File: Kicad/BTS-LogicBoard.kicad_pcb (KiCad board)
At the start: 2 copper layers, 41.9 x 55.9 mm, 52 parts, among them J1 Conn_01x06, J2 Conn_01x04, J3 Conn_01x02, Q1 BC817, Q2 BC807, Q3 BC817, Q4 BC807, Q5 BC817, Q6 BC817, SW1 SW_DPDT_x2, SW2 SW_DPDT_x2, U1 NCS2252SN2T1G, U2 NE555D, U3 NCS2252SN2T1G

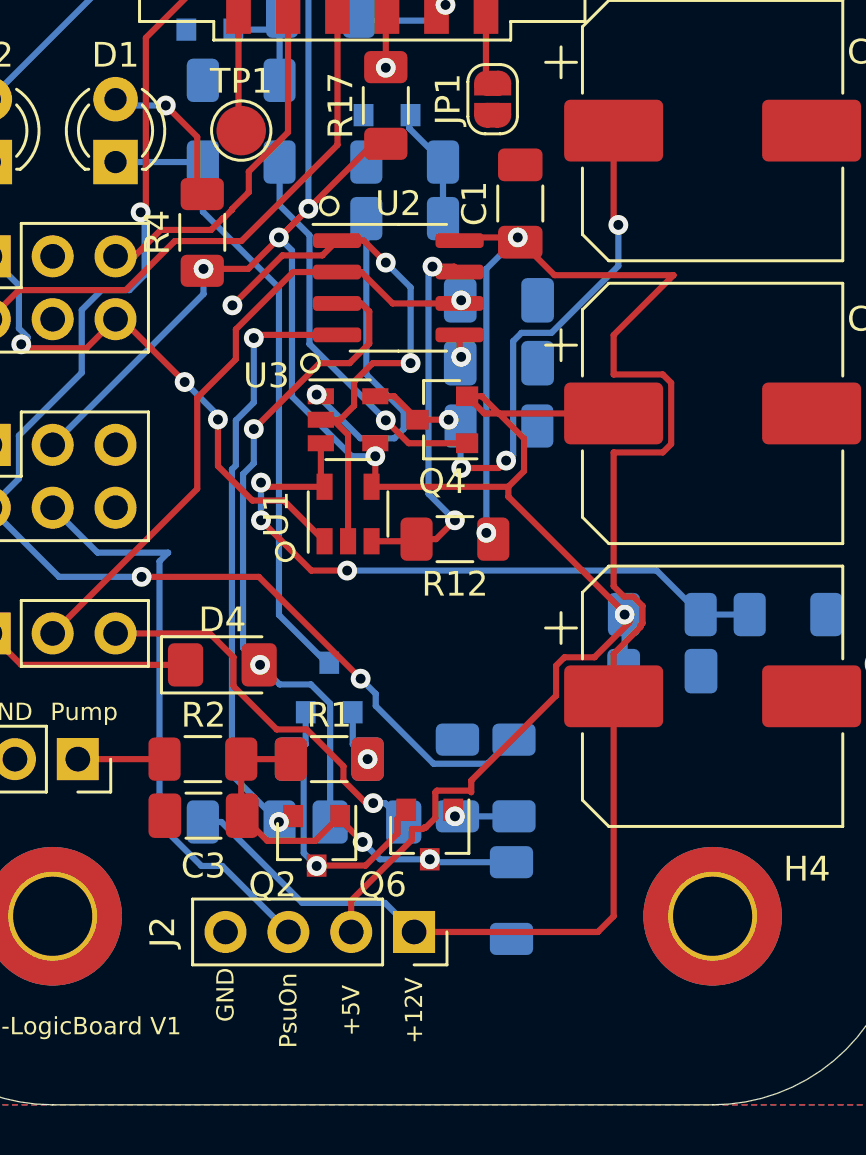
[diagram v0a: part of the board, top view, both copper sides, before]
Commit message: Updated silkscreen and Gerbers
Signed-off-by: bebenlebricolo <benoittarrade@hotmail.fr>
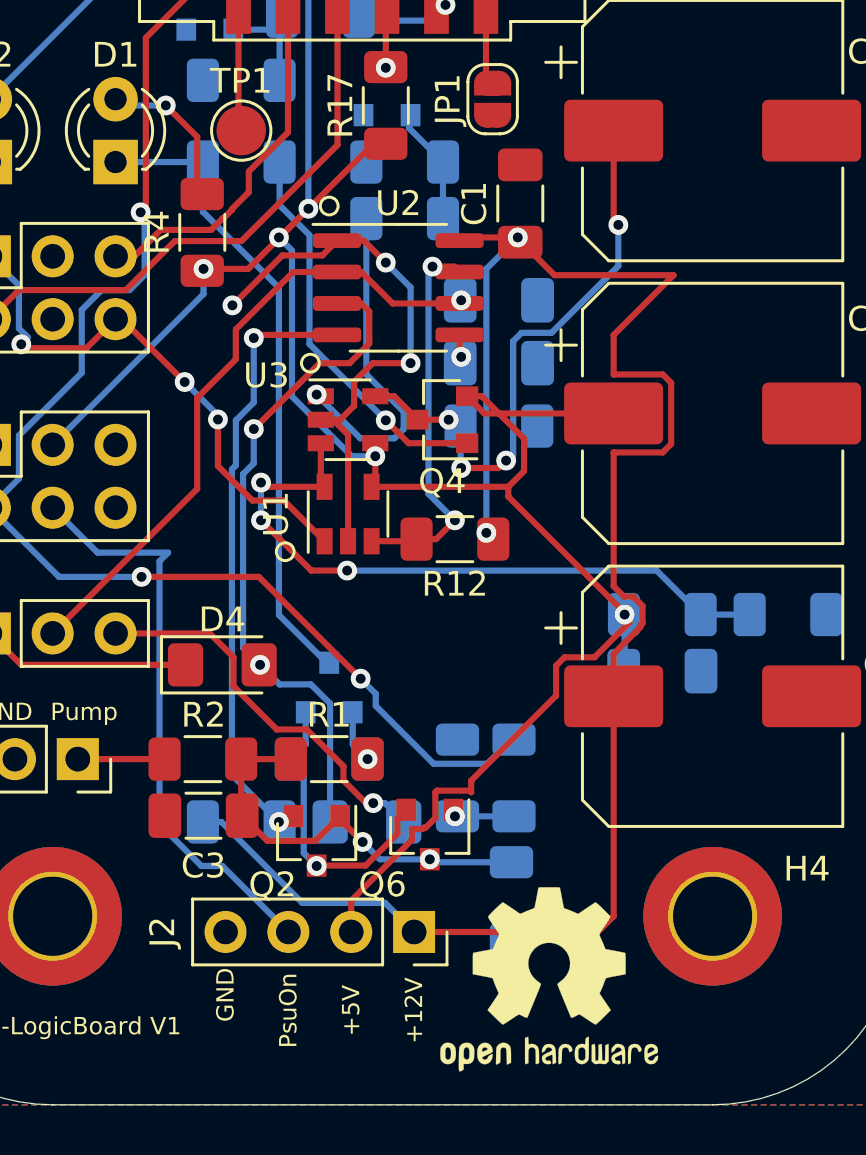
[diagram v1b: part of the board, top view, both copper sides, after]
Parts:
- added REF**: OSHW-Logo2_9.8x8mm_SilkScreen, Symbol:OSHW-Logo2_9.8x8mm_SilkScreen, B.Cu at (141.0, 81.5)
- added REF**: OSHW-Logo2_9.8x8mm_SilkScreen, Symbol:OSHW-Logo2_9.8x8mm_SilkScreen, F.Cu at (139.4, 116.8)

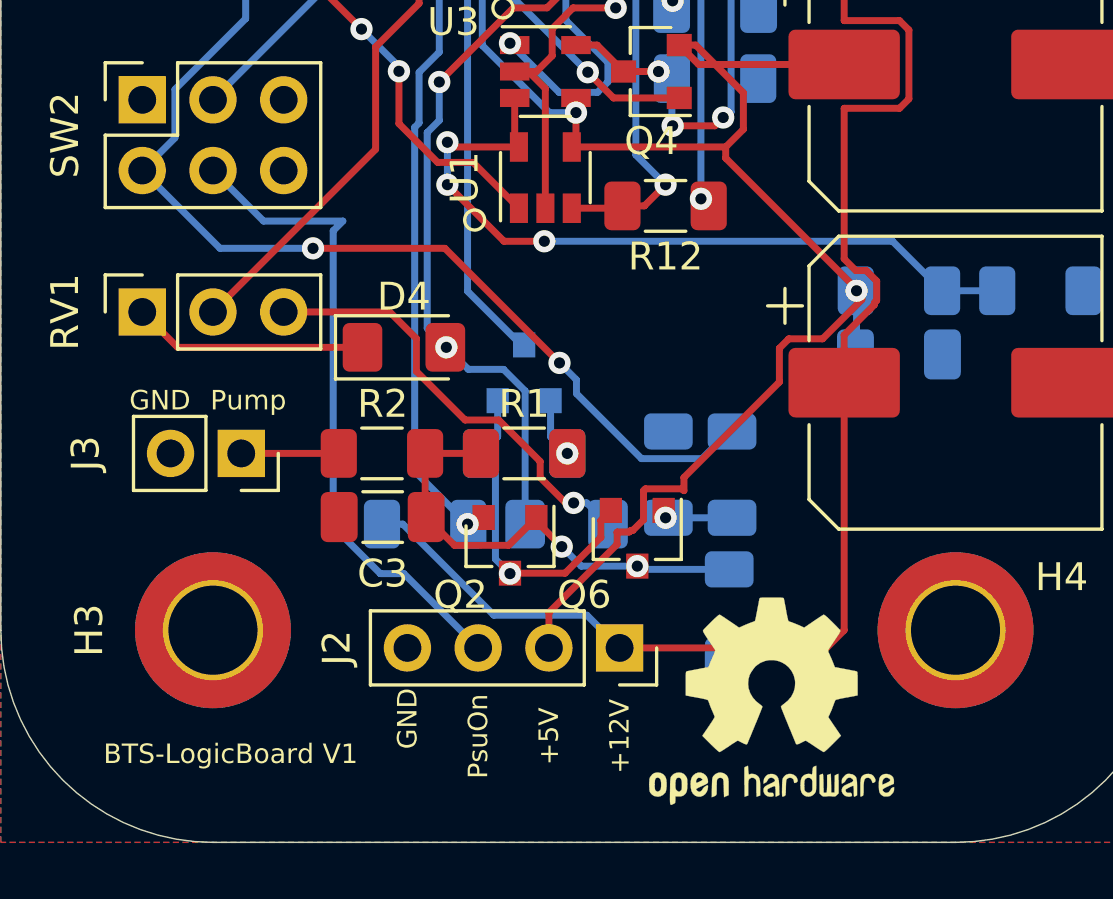
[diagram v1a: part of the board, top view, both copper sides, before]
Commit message: Updated board with optocoupler
Signed-off-by: bebenlebricolo <benoittarrade@hotmail.fr>
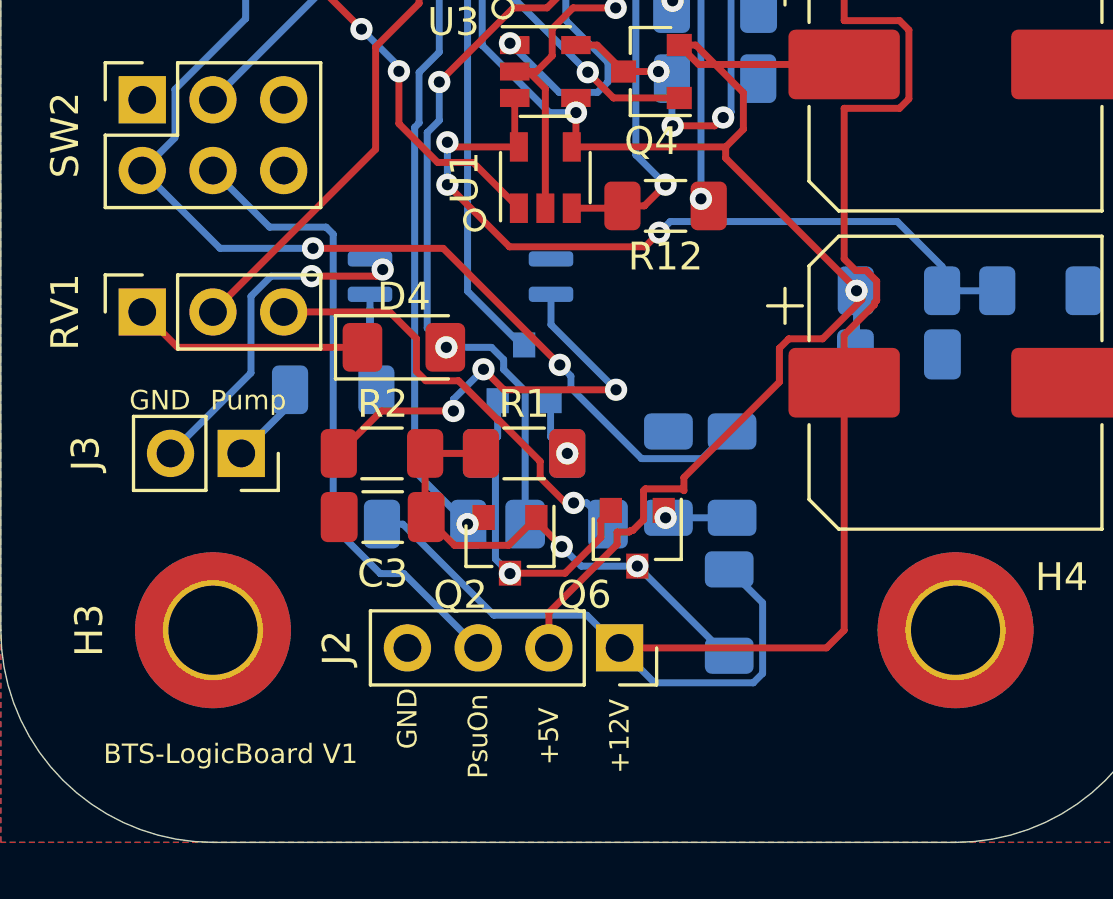
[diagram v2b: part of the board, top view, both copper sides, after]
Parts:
- removed REF** (x2): OSHW-Logo2_9.8x8mm_SilkScreen, Symbol:OSHW-Logo2_9.8x8mm_SilkScreen
- added R20: 1k, Resistor_SMD:R_1206_3216Metric_Pad1.30x1.75mm_HandSolder, B.Cu at (123.7, 105.7)
- added U4: TLP291, Package_SO:SOIC-4_4.55x2.6mm_P1.27mm, B.Cu at (128.3, 101.6)
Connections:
- J3 pad 2: GND -> GND1
- R2 pad 2: /Pump-On -> Net-(R2-Pad2)
- R5 pad 1: /PWM_Enable -> +12V
- R5 pad 2: GND -> /PWM_Enable
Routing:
- net Net-(R2-Pad2): track 0.00 -> 16.2 mm, vias 0 -> 3
- net GND1: track 0.00 -> 12.6 mm, vias 0 -> 2
- net +12V: track 73.2 -> 83.3 mm
- net Net-(R20-Pad1): track 0.00 -> 6.22 mm
- net /PWM_Enable: track 16.9 -> 18.3 mm
- net /2.5V: track 27.3 -> 28.6 mm
- net /PSU_ON: track 23.5 -> 22.8 mm

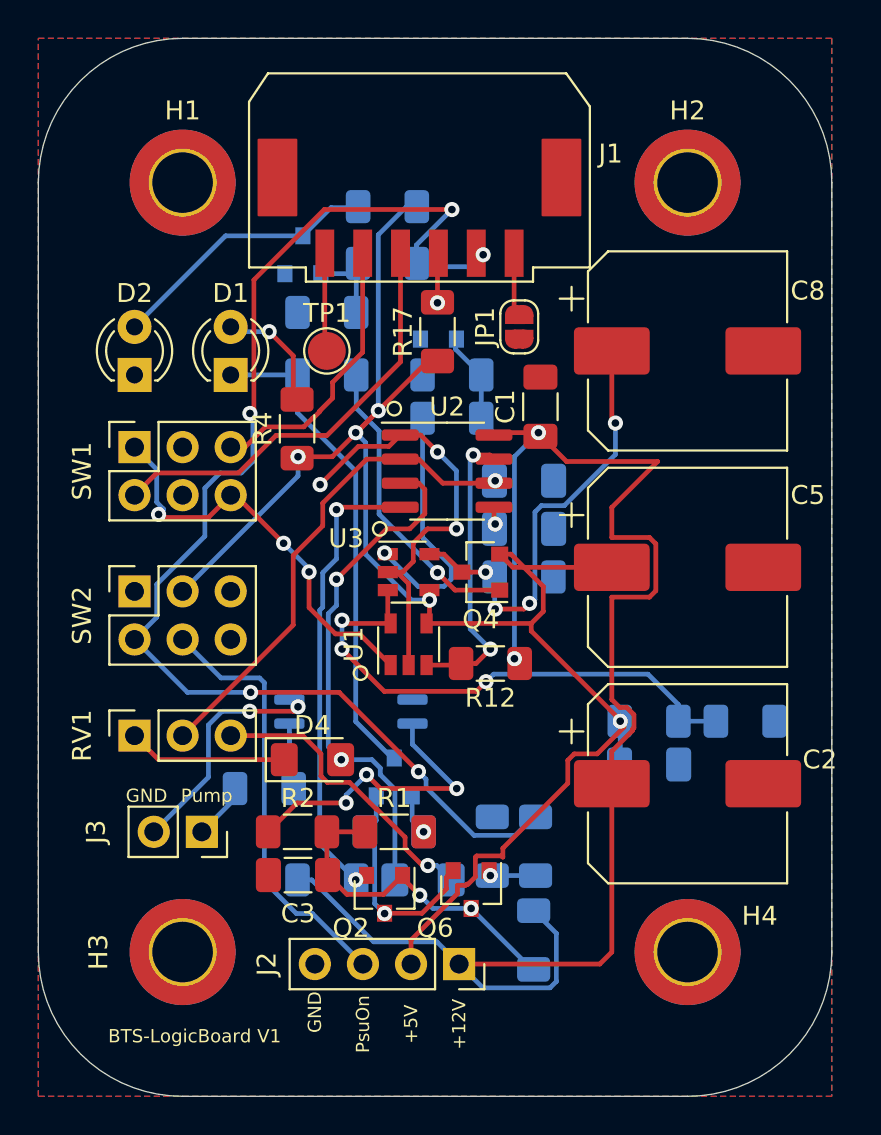
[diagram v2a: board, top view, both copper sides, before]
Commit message: Fixed unatural DPDT switch mapping
Signed-off-by: bebenlebricolo <benoittarrade@hotmail.fr>
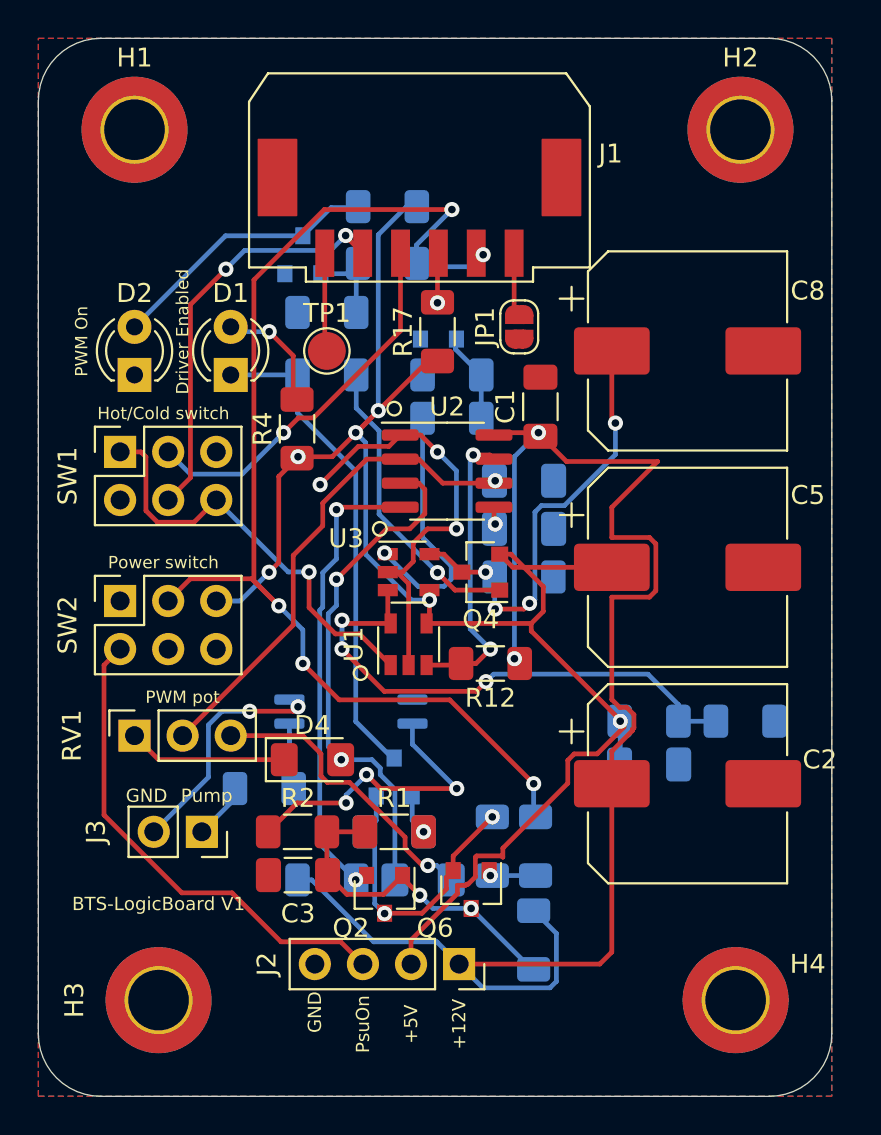
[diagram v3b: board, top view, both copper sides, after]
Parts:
- SW1, SW2: footprint Connector_PinSocket_2.54mm:PinSocket_2x03_P2.54mm_Vertical -> BTS-LogicBoard:PinSocket_2x03_P2.54mm_Vertical_DPDT_Special
- moved H2 3.95 mm to (148.8, 70.9)
- moved H1 3.78 mm to (116.8, 70.9)
- moved H4 3.59 mm to (148.6, 116.8)
- moved H3 2.84 mm to (118.1, 116.8)
- moved SW2 0.92 mm to (116.1, 95.8)
- moved SW1 0.80 mm to (116.1, 87.9)
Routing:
- net /IN-: track 14.8 -> 21.8 mm, vias 0 -> 2
- net GND: track 34.4 -> 38.1 mm, vias 4 -> 5
- net /HIP_DISABLE: track 68.4 -> 64.9 mm
- net /PSU_ON: track 22.8 -> 26.1 mm
- net /IN+: track 22.7 -> 20.0 mm, vias 0 -> 1
- net /COMP-Out: track 22.0 -> 22.9 mm, vias 3 -> 1
- net +5V: track 92.2 -> 92.6 mm, vias 5 -> 6
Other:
- outline, holes or cut-outs redrawn
- board text added: "Driver Enabled"
- board text added: "Hot/Cold switch"
- board text added: "PWM On"
- board text added: "PWM pot"
- board text added: "Power switch"

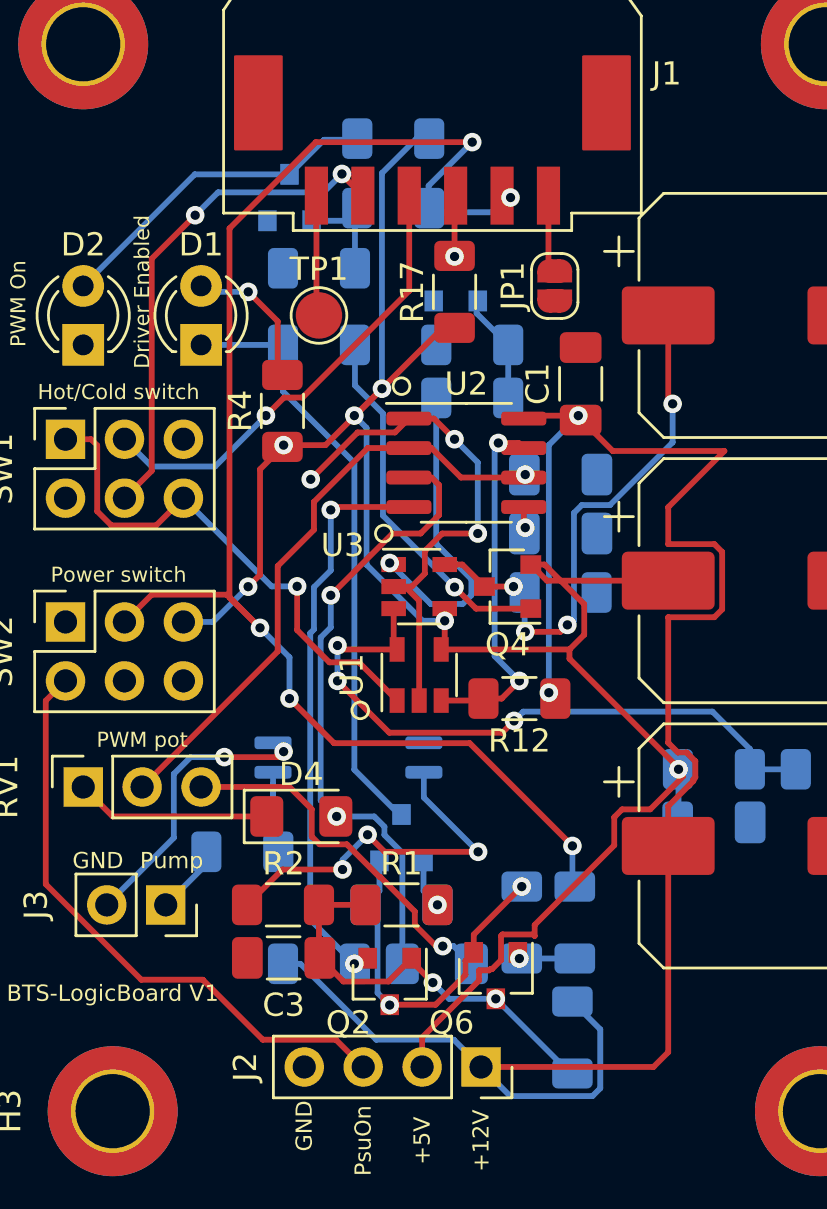
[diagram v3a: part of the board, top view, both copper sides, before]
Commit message: Swapped 12Vcc on NE555 outputs and remapped comparators
Signed-off-by: bebenlebricolo <benoittarrade@hotmail.fr>
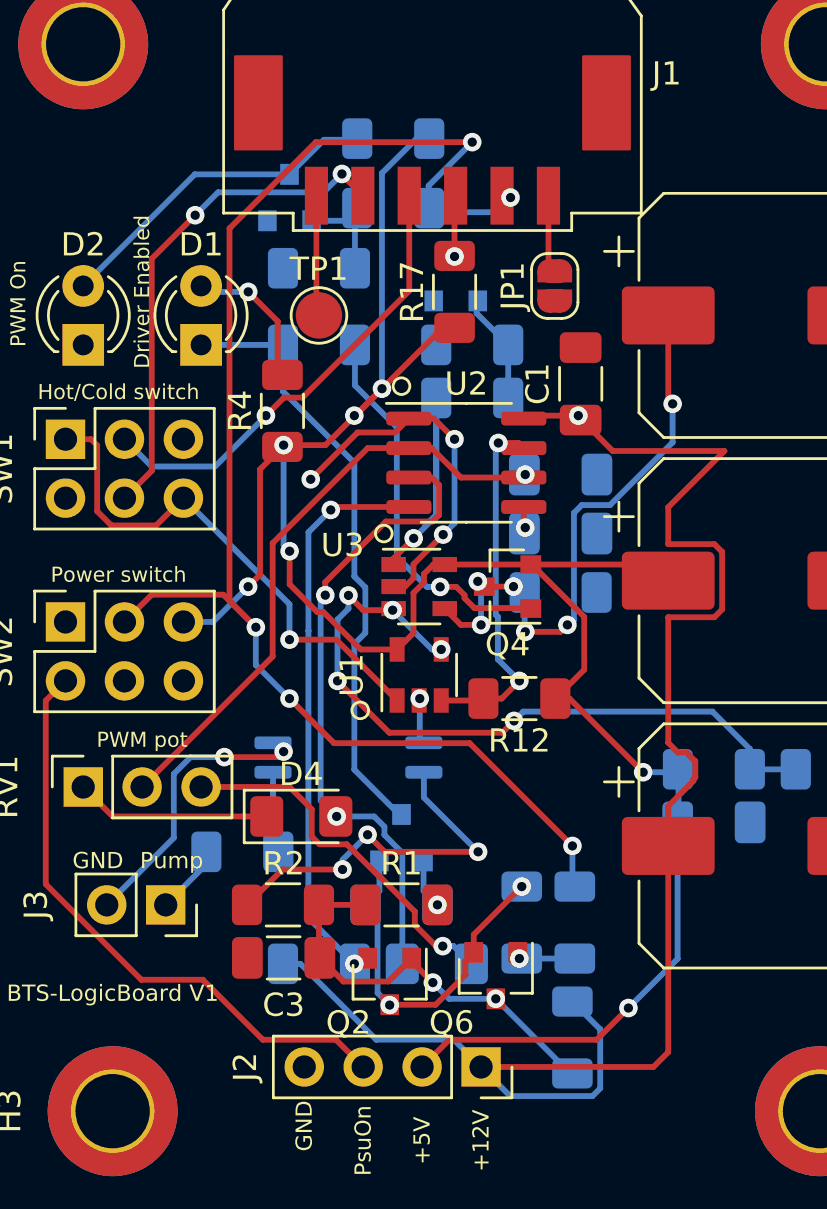
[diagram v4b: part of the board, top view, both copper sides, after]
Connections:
- R12 pad 1: +12V -> +5V
- U1 pad 4: +5V -> /2.5V
- U1 pad 5: /2.5V -> +5V
- U3 pad 4: +5V -> Net-(C8-Pad1)
- U3 pad 5: Net-(C8-Pad1) -> +5V
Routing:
- net +12V: track 83.3 -> 70.4 mm, vias 2 -> 1
- net GND: track 38.1 -> 32.6 mm, vias 5 -> 6
- net /2.5V: track 28.6 -> 31.5 mm, vias 3 -> 5
- net +5V: track 92.6 -> 95.1 mm, vias 6 -> 7
- net Net-(C8-Pad1): track 23.8 -> 25.2 mm, vias 4 -> 6
- net Net-(Q4-Pad1): track 15.9 -> 16.7 mm
